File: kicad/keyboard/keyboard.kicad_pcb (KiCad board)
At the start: 2 copper layers, 141 parts, among them K1 KEYSW, K2 KEYSW, K3 KEYSW, K4 KEYSW, K5 KEYSW, K6 KEYSW, U1 IS31FL3733-TQ

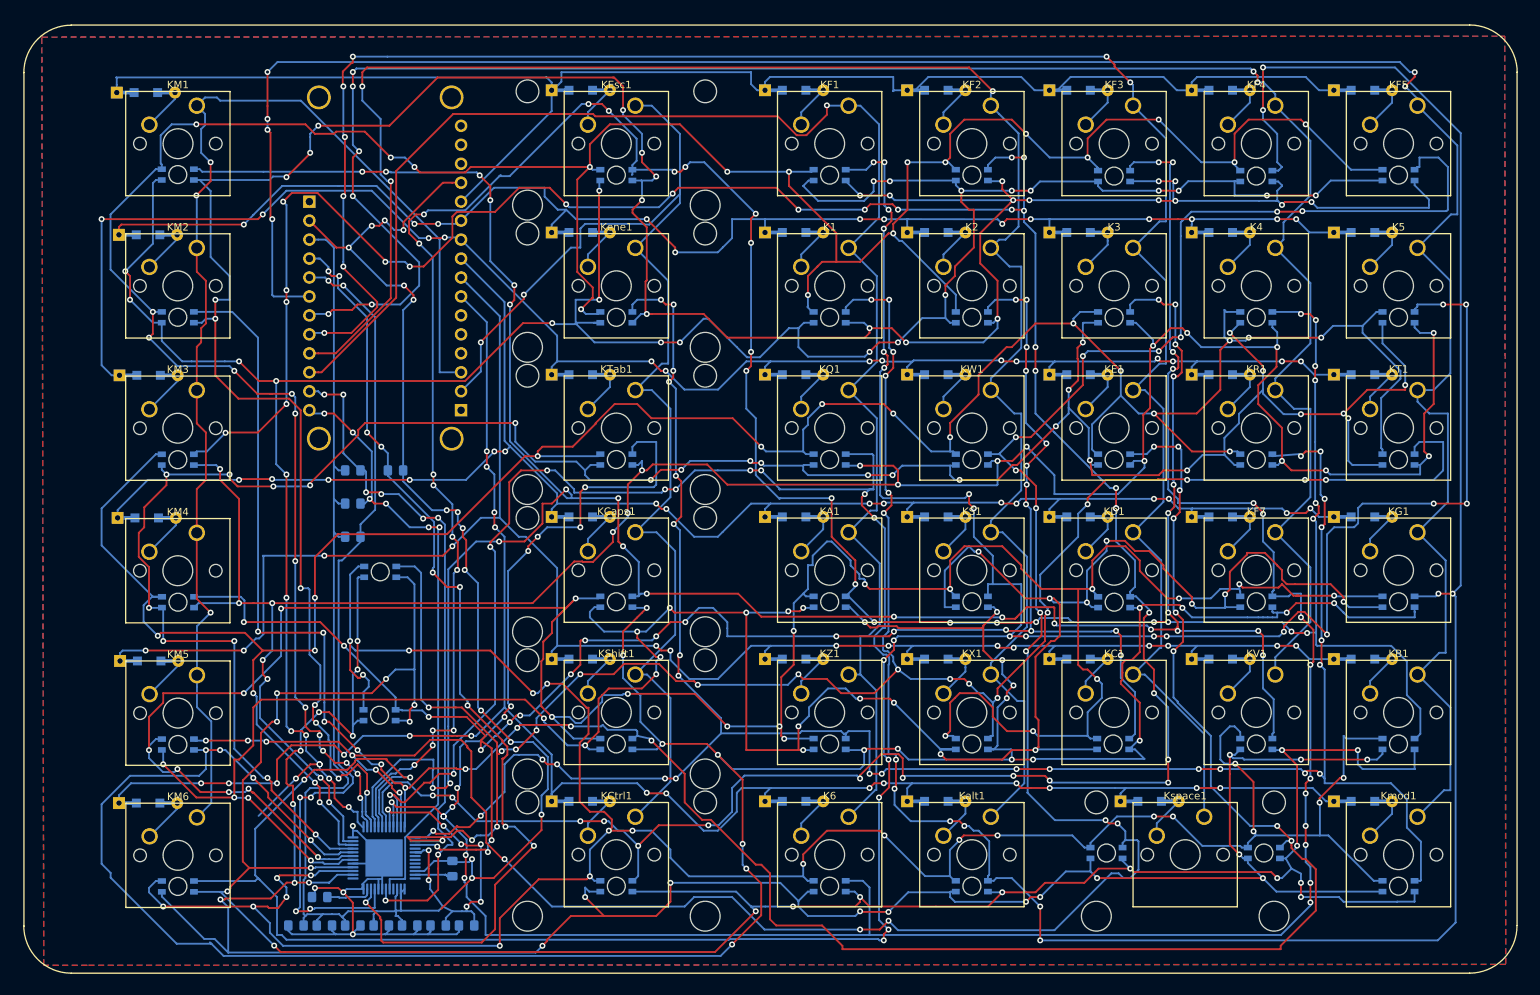
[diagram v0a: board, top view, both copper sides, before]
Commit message: fixed borders, added text to pcb
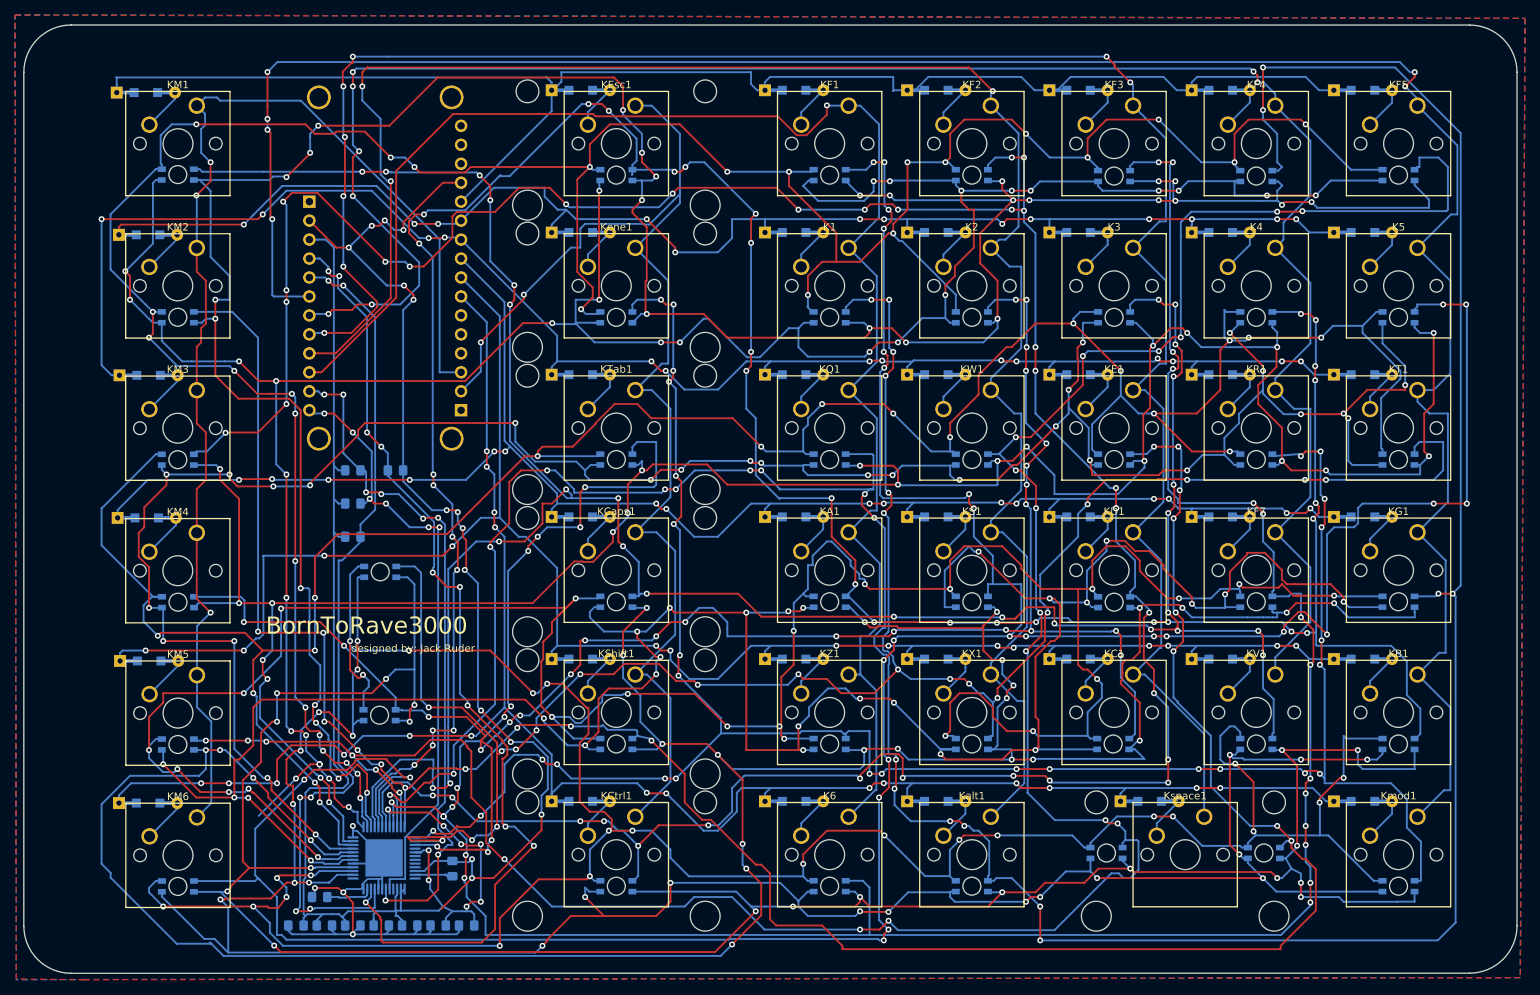
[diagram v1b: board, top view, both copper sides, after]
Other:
- board outline added: 200 x 127 mm
- board text added: "BornToRave3000"
- board text added: "designed by: Jack Ruder"
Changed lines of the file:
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@@
   (general
     (thickness 1.6)
-    (drawings 8)
+    (drawings 10)
     (tracks 4236)
     (zones 0)
@@
     (32 B.Adhes user)
     (33 F.Adhes user)
-    (34 B.Paste user)
+    (34 B.Paste user hide)
     (35 F.Paste user)
     (36 B.SilkS user hide)
@@
     )
   )
-  (gr_arc (start 53.0987 47.6885) (end 53.0987 41.3258) (angle -90) (layer F.SilkS) (width 0.12))
-  (gr_arc (start 53.086 161.9504) (end 46.7233 161.9504) (angle -90) (layer F.SilkS) (width 0.12))
-  (gr_arc (start 240.3856 161.9504) (end 240.3856 168.3131) (angle -90) (layer F.SilkS) (width 0.12))
-  (gr_arc (start 240.411 47.6631) (end 246.7737 47.6631) (angle -90) (layer F.SilkS) (width 0.12))
-  (gr_line (start 246.7483 161.925) (end 246.7483 47.625) (layer F.SilkS) (width 0.12))
-  (gr_line (start 46.7487 47.6631) (end 46.7487 162.052) (layer F.SilkS) (width 0.12))
-  (gr_line (start 240.411 41.3131) (end 53.07838 41.3131) (layer F.SilkS) (width 0.12))
-  (gr_line (start 53.0987 168.3131) (end 240.3983 168.3131) (layer F.SilkS) (width 0.12))
+  (gr_text "designed by: Jack Ruder" (at 98.8568 124.8156) (layer F.SilkS)
+    (effects (font (size 1 1) (thickness 0.15)))
+  )
+  (gr_text BornToRave3000 (at 92.6592 121.7676) (layer F.SilkS)
+    (effects (font (size 2.286 2.286) (thickness 0.254)))
+  )
+  (gr_arc (start 53.0606 162.0012) (end 46.736 162.052) (angle -89.1) (layer Edge.Cuts) (width 0.12))
+  (gr_arc (start 53.086 47.6504) (end 53.086 41.3004) (angle -90) (layer Edge.Cuts) (width 0.12))
+  (gr_line (start 46.736 47.6504) (end 46.736 162.052) (layer Edge.Cuts) (width 0.12))
+  (gr_line (start 240.407722 41.313051) (end 53.086 41.3004) (layer Edge.Cuts) (width 0.12))
+  (gr_line (start 53.012051 168.325818) (end 240.3856 168.3131) (layer Edge.Cuts) (width 0.12))
+  (gr_line (start 246.7483 161.9504) (end 246.748299 47.625001) (layer Edge.Cuts) (width 0.12))
+  (gr_arc (start 240.411 47.6504) (end 246.748299 47.625001) (angle -89.8) (layer Edge.Cuts) (width 0.12))
+  (gr_arc (start 240.3856 161.9504) (end 240.3856 168.3131) (angle -90) (layer Edge.Cuts) (width 0.12))
   (via (at 85.725 156.905) (size 0.8) (drill 0.4) (layers F.Cu B.Cu) (net 1))
   (segment (start 85.725 157.725) (end 85.335 158.115) (width 0.25) (layer B.Cu) (net 1))
@@
     (polygon
       (pts
-        (xy 245.237 167.132) (xy 55.245 167.259) (xy 49.403 167.259) (xy 49.149 42.926) (xy 245.11 42.799)
+        (xy 247.1928 168.91) (xy 54.8386 169.1894) (xy 45.72 169.0878) (xy 45.5422 39.9796) (xy 247.8278 40.4114)
       )
     )
@@
     (polygon
       (pts
-        (xy 245.237 167.132) (xy 55.245 167.259) (xy 49.403 167.259) (xy 49.149 42.926) (xy 245.11 42.799)
+        (xy 247.1928 168.91) (xy 55.0164 169.164) (xy 45.72 169.1894) (xy 45.5676 39.9542) (xy 247.8278 40.4114)
       )
     )
